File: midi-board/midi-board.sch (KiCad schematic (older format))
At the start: 39 parts, among them J1 MIDI OUT, J2 MIDI IN, J3 Qwiic, J4 A0, J5 A1, J6 Qwiic, J7 UART, U1 74LVC1G06, U2 74LVC1G17, U3 TLP185(SE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

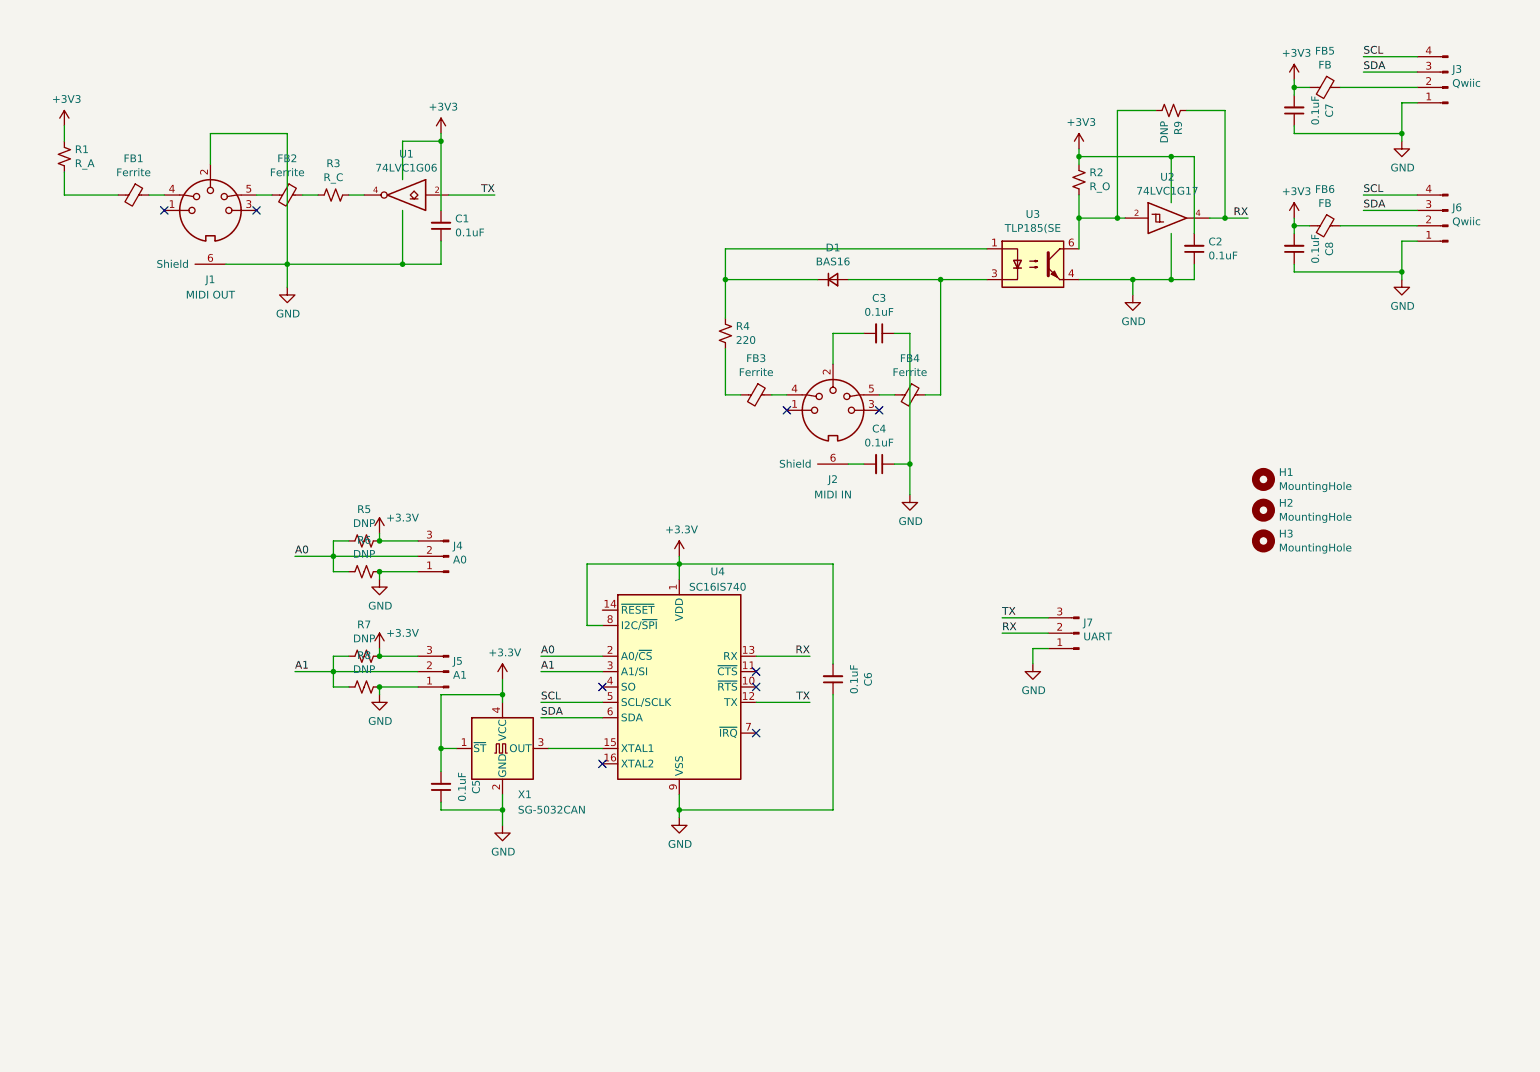
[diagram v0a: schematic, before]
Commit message: alternate uart symbol for the midi board. not sure why i did this
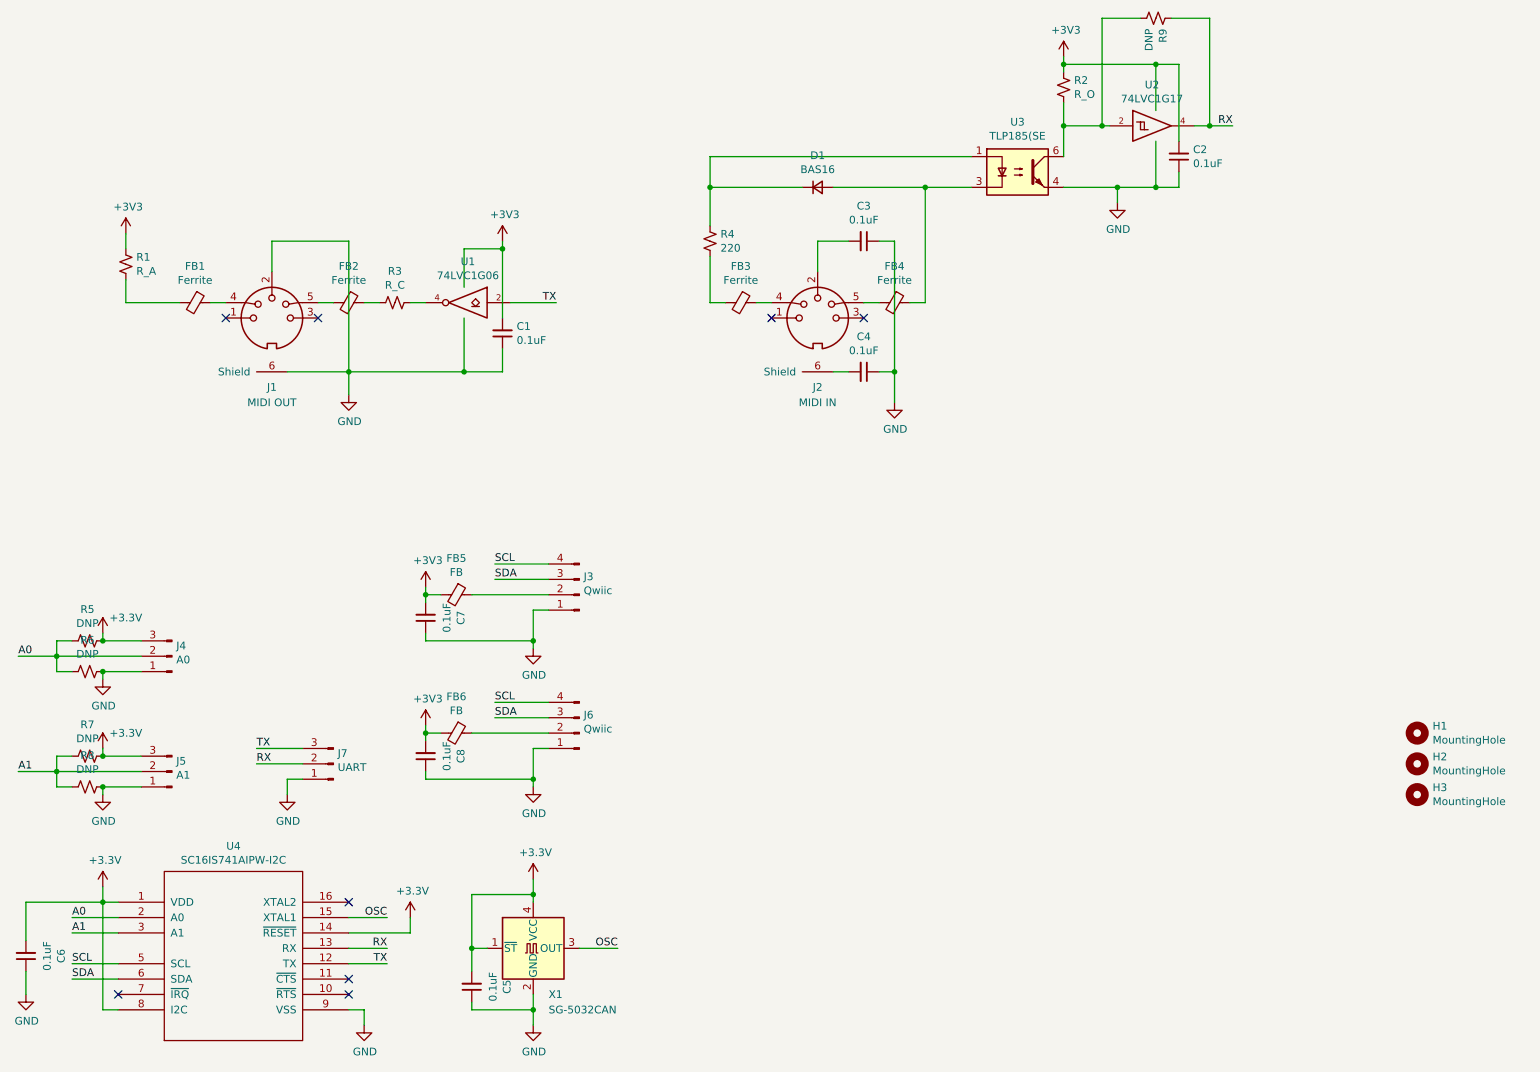
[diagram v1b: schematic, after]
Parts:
- removed U4: SC16IS740, Housings_SSOP:TSSOP-16_4.4x5mm_Pitch0.65mm, symbol Interface_UART:SC16IS740
- added U4: SC16IS741AIPW-I2C, Housings_SSOP:TSSOP-16_4.4x5mm_Pitch0.65mm, symbol SC16IS741AIPW_I2C:SC16IS741AIPW-I2C
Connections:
- net +3V3: now also U4.1 (VDD), U4.14 (~RESET), U4.8 (I2C)
- net A0: now also U4.2 (A0)
- net A1: now also U4.3 (A1)
- net GND: now also U4.9 (VSS)
- net RX: now also U4.13 (RX)
- net SCL: now also U4.5 (SCL)
- net SDA: now also U4.6 (SDA)
- net TX: now also U4.12 (TX)
- net OSC: now reaches X1.3 (OUT)
- net OSC: now also U4.15 (XTAL1)
- no-connect marks 9 -> 8
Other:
- moved on the sheet: C1, C2, C3, C4, C5, C6, C7, C8, D1, FB1, FB2, FB3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
